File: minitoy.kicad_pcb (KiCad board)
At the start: 4 copper layers, 71 parts, among them J1 Conn_01x06, J2 PMOD1, J3 PMOD2, J4 USB_B_Micro, SW1 SW_Push, SW2 SW_Push, SW3 SW_Push, SW4 SW_Push, U1 ICE40UP5K-SG48, U2 ESP-12E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

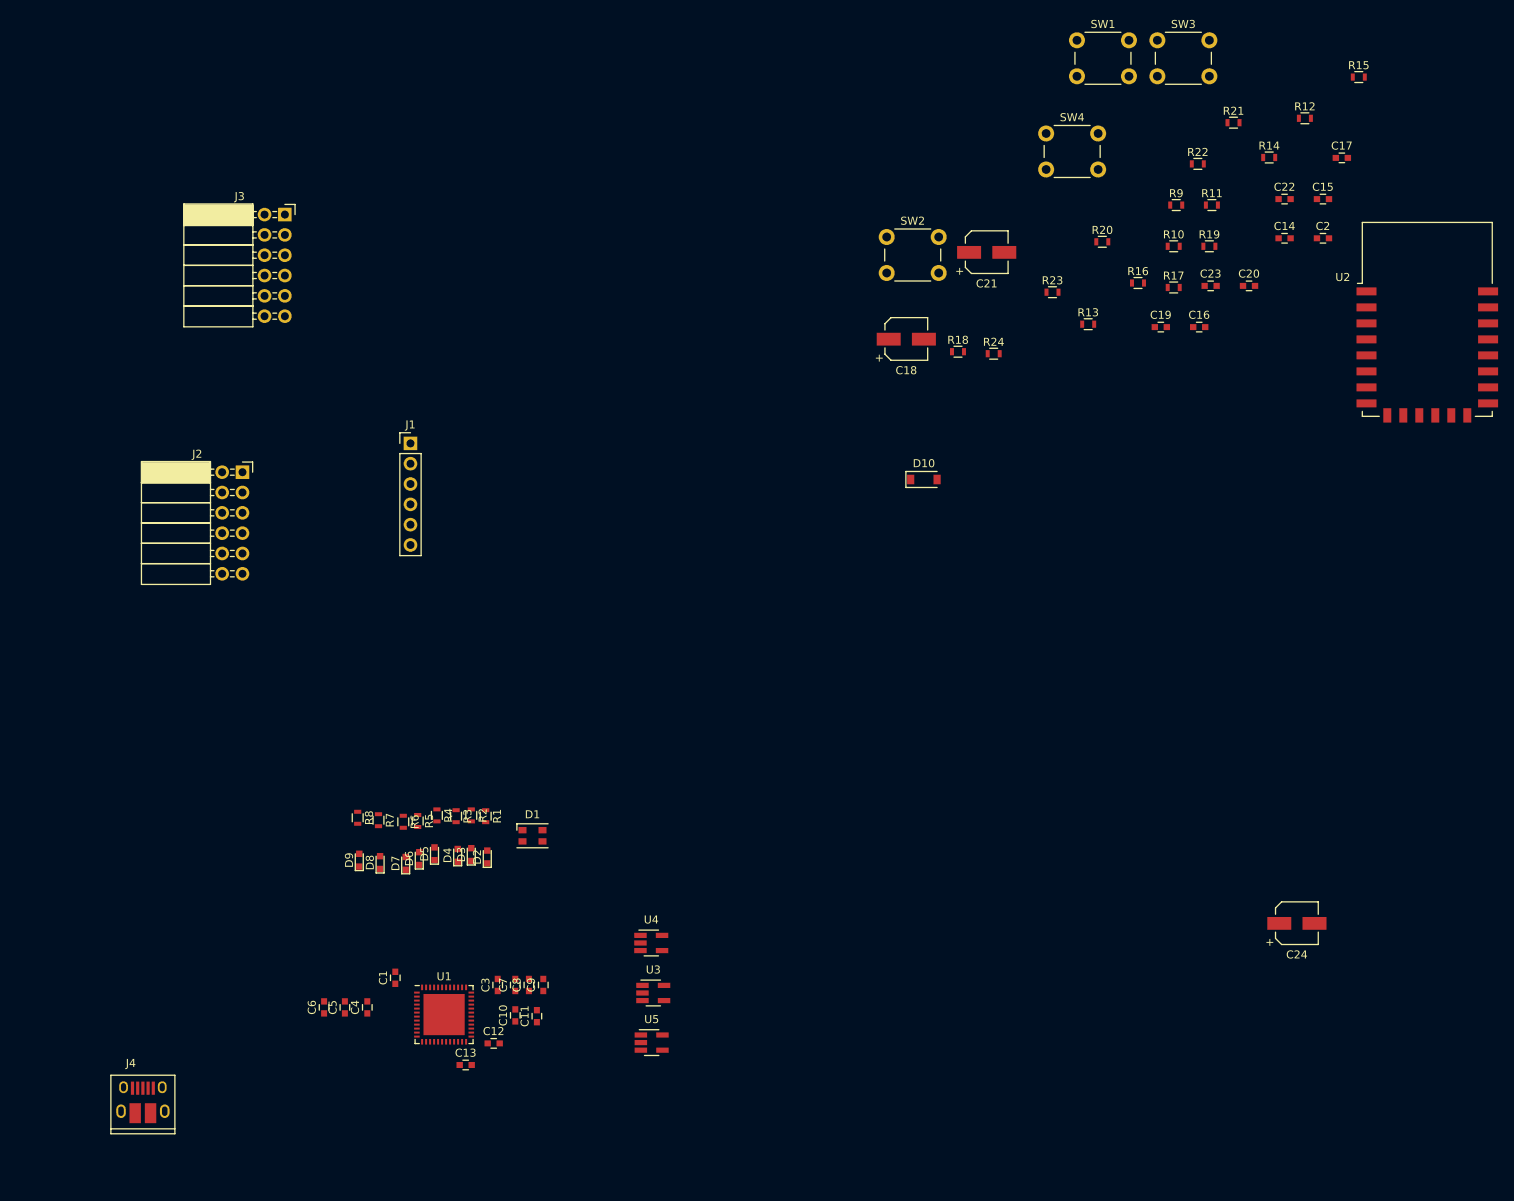
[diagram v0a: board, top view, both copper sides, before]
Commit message: Remove blinkenlights and buttons, add another PMOD socket
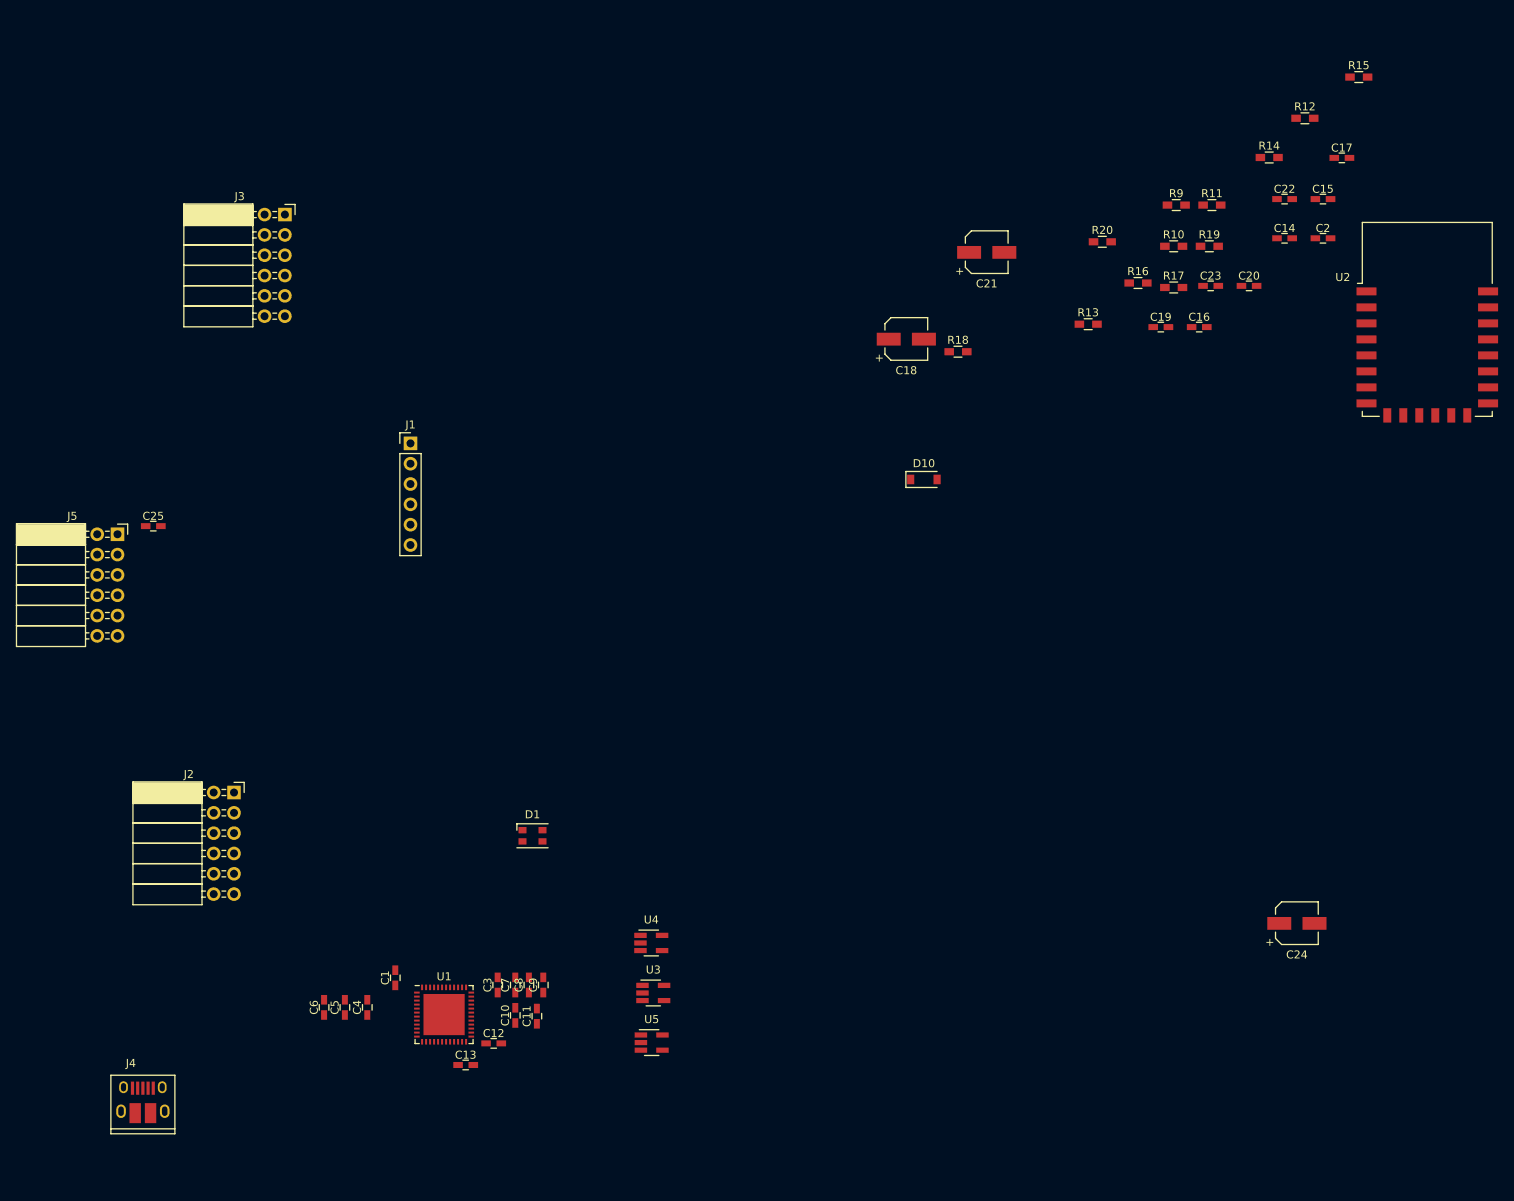
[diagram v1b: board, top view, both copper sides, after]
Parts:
- removed D2, D3, D4, D5, D6, D7, D8, D9: LED, LEDs:LED_0603
- removed R1, R2, R3, R4, R5, R6, R7, R8: 270, Resistors_SMD:R_0603
- removed R21, R22, R23, R24: 10k, Resistors_SMD:R_0603
- removed SW1, SW2, SW3, SW4: SW_Push, Buttons_Switches_THT:SW_PUSH_6mm
- added C25: 0.1uF, Capacitors_SMD:C_0603_HandSoldering, F.Cu at (81.4, 70.8)
- added J5: PMOD3, Socket_Strips:Socket_Strip_Angled_2x06_Pitch2.54mm, F.Cu at (76.9, 71.9)
- C1, C10, C11, C12, C13, C14, C15, C16, C17, C19, C2, C20, C22, C23, C3, C4, C5, C6, C7, C8, C9: footprint Capacitors_SMD:C_0603 -> Capacitors_SMD:C_0603_HandSoldering
- R10, R11, R12, R13, R14, R15, R16, R17, R18, R19, R20, R9: footprint Resistors_SMD:R_0603 -> Resistors_SMD:R_0603_HandSoldering
- moved J2 40.1 mm to (91.4, 104.1)
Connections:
- J1 pad 2: Net-(J1-Pad2) -> (no net)
- J1 pad 3: Net-(J1-Pad3) -> (no net)
- J4 pad 2: Net-(J4-Pad2) -> (no net)
- J4 pad 3: Net-(J4-Pad3) -> (no net)
- J4 pad 4: Net-(J4-Pad4) -> (no net)
- U1 pad 10: PMOD-1.3 -> PMOD-2.3
- U1 pad 11: PMOD-1.4 -> PMOD-2.4
- U1 pad 12: PMOD-1.7 -> PMOD-2.7
- U1 pad 13: PMOD-1.8 -> PMOD-2.8
- U1 pad 18: PMOD-1.9 -> PMOD-2.9
- U1 pad 19: PMOD-1.10 -> PMOD-2.10
- U1 pad 2: FPGA_LED_0 -> PMOD-3.3
- U1 pad 23: PMOD-2.7 -> PMOD-1.7
- U1 pad 25: PMOD-2.1 -> PMOD-1.1
- U1 pad 26: PMOD-2.8 -> PMOD-1.8
- U1 pad 27: PMOD-2.2 -> PMOD-1.2
- U1 pad 3: FPGA_LED_1 -> PMOD-3.2
- U1 pad 31: PMOD-2.3 -> PMOD-1.3
- U1 pad 32: PMOD-2.9 -> PMOD-1.9
- U1 pad 34: PMOD-2.4 -> PMOD-1.4
- U1 pad 35: BTN0 -> (no net)
- U1 pad 36: BTN1 -> (no net)
- U1 pad 37: PMOD-2.10 -> PMOD-1.10
- U1 pad 38: BTN2 -> (no net)
- U1 pad 4: FPGA_LED_2 -> PMOD-3.1
- U1 pad 42: BTN3 -> (no net)
- U1 pad 43: Net-(U1-Pad43) -> (no net)
- U1 pad 44: FPGA_LED_3 -> PMOD-3.10
- U1 pad 45: FPGA_LED_4 -> PMOD-3.9
- U1 pad 46: FPGA_LED_5 -> PMOD-3.8
- U1 pad 47: FPGA_LED_6 -> PMOD-3.7
- U1 pad 48: FPGA_LED_7 -> PMOD-3.4
- U1 pad 6: PMOD-1.1 -> PMOD-2.1
- U1 pad 9: PMOD-1.2 -> PMOD-2.2
- U2 pad 1: Net-(U2-Pad1) -> (no net)
- U2 pad 10: Net-(U2-Pad10) -> (no net)
- U2 pad 11: Net-(U2-Pad11) -> (no net)
- U2 pad 12: Net-(U2-Pad12) -> (no net)
- U2 pad 13: Net-(U2-Pad13) -> (no net)
- U2 pad 14: Net-(U2-Pad14) -> (no net)
- U2 pad 2: Net-(U2-Pad2) -> (no net)
- U2 pad 9: Net-(U2-Pad9) -> (no net)
- U3 pad 4: Net-(U3-Pad4) -> (no net)
- U4 pad 4: Net-(U4-Pad4) -> (no net)
- U5 pad 4: Net-(U5-Pad4) -> (no net)

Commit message: More consolidation of the board
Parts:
- U2: moved to B.Cu
- moved R15 170.7 mm to (123.6, 146.5), turned to 90 degrees
- moved U2 147.4 mm to (127.1, 139.1), turned to 90 degrees
- moved R12 145.6 mm to (131.4, 131.2), turned to 90 degrees
- moved R9 139.3 mm to (131.7, 146.4), turned to 90 degrees
- moved R14 135.7 mm to (122.7, 118.5)
- moved R19 135.6 mm to (125.3, 139.1), turned to 90 degrees
- moved R17 133.3 mm to (127.4, 146.4), turned to 90 degrees
- moved R11 131.1 mm to (129.4, 131.2), turned to 90 degrees
- moved R10 130.3 mm to (129.7, 139.3), turned to 270 degrees
- moved C21 124.1 mm to (106.3, 132.1), turned to 270 degrees
- moved R20 123.9 mm to (121.5, 131.2), turned to 270 degrees
- moved R13 122.2 mm to (129.4, 146.6), turned to 90 degrees
- moved R16 121.5 mm to (123.6, 131.2), turned to 90 degrees
- moved R18 115.1 mm to (120.7, 146.5), turned to 90 degrees
- moved C24 107.1 mm to (117.9, 132.1), turned to 270 degrees
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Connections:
- J1 pad 2: (no net) -> Net-(J1-Pad2)
- J1 pad 3: (no net) -> Net-(J1-Pad3)
- J2 pad 10: PMOD-1.10 -> GND
- J2 pad 11: GND -> +3V3
- J2 pad 2: PMOD-1.2 -> PMOD-1.7
- J2 pad 3: PMOD-1.3 -> PMOD-1.2
- J2 pad 4: PMOD-1.4 -> PMOD-1.8
- J2 pad 5: GND -> PMOD-1.3
- J2 pad 6: +3V3 -> PMOD-1.9
- J2 pad 7: PMOD-1.7 -> PMOD-1.4
- J2 pad 8: PMOD-1.8 -> PMOD-1.10
- J2 pad 9: PMOD-1.9 -> GND
- J3 pad 10: PMOD-2.10 -> GND
- J3 pad 11: GND -> +3V3
- J3 pad 2: PMOD-2.2 -> PMOD-2.7
- J3 pad 3: PMOD-2.3 -> PMOD-2.2
- J3 pad 4: PMOD-2.4 -> PMOD-2.8
- J3 pad 5: GND -> PMOD-2.3
- J3 pad 6: +3V3 -> PMOD-2.9
- J3 pad 7: PMOD-2.7 -> PMOD-2.4
- J3 pad 8: PMOD-2.8 -> PMOD-2.10
- J3 pad 9: PMOD-2.9 -> GND
- J4 pad 2: (no net) -> Net-(J4-Pad2)
- J4 pad 3: (no net) -> Net-(J4-Pad3)
- J4 pad 4: (no net) -> Net-(J4-Pad4)
- J5 pad 10: PMOD-3.10 -> GND
- J5 pad 11: GND -> +3V3
- J5 pad 2: PMOD-3.2 -> PMOD-3.7
- J5 pad 3: PMOD-3.3 -> PMOD-3.2
- J5 pad 4: PMOD-3.4 -> PMOD-3.8
- J5 pad 5: GND -> PMOD-3.3
- J5 pad 6: +3V3 -> PMOD-3.9
- J5 pad 7: PMOD-3.7 -> PMOD-3.4
- J5 pad 8: PMOD-3.8 -> PMOD-3.10
- J5 pad 9: PMOD-3.9 -> GND
- U1 pad 2: PMOD-3.3 -> PMOD-3.8
- U1 pad 3: PMOD-3.2 -> PMOD-3.9
- U1 pad 35: (no net) -> Net-(U1-Pad35)
- U1 pad 36: (no net) -> Net-(U1-Pad36)
- U1 pad 38: (no net) -> Net-(U1-Pad38)
- U1 pad 4: PMOD-3.1 -> PMOD-3.10
- U1 pad 42: (no net) -> Net-(U1-Pad42)
- U1 pad 43: (no net) -> Net-(U1-Pad43)
- U1 pad 44: PMOD-3.10 -> PMOD-3.1
- U1 pad 45: PMOD-3.9 -> PMOD-3.2
- U1 pad 46: PMOD-3.8 -> PMOD-3.3
- U1 pad 47: PMOD-3.7 -> PMOD-3.4
- U1 pad 48: PMOD-3.4 -> PMOD-3.7
- U2 pad 1: (no net) -> Net-(U2-Pad1)
- U2 pad 10: (no net) -> Net-(U2-Pad10)
- U2 pad 11: (no net) -> Net-(U2-Pad11)
- U2 pad 12: (no net) -> Net-(U2-Pad12)
- U2 pad 13: (no net) -> Net-(U2-Pad13)
- U2 pad 14: (no net) -> Net-(U2-Pad14)
- U2 pad 2: (no net) -> Net-(U2-Pad2)
- U2 pad 9: (no net) -> Net-(U2-Pad9)
- U3 pad 4: (no net) -> Net-(U3-Pad4)
- U4 pad 4: (no net) -> Net-(U4-Pad4)
- U5 pad 4: (no net) -> Net-(U5-Pad4)
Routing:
- net +1V2: track 0.00 -> 7.74 mm
- net PMOD-1.9: track 0.00 -> 7.61 mm
- net PMOD-1.3: track 0.00 -> 7.55 mm
- net +3V3: track 0.00 -> 3.07 mm
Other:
- board outline added: 47.2 x 45 mm
- net class Default: clearance 0.254 -> 0.1524; trace_width 0.254 -> 0.1524
- net class PWR added: clearance 0.254, trace_width 0.508, via_dia 0.762, via_drill 0.4064
- rule trace_clearance: 0.254 -> 0.1524
